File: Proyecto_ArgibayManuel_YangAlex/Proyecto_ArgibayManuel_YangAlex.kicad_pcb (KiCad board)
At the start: 2 copper layers, 60 parts, among them IC1 LM1117, J1 Conn_01x01, J2 Con_1x2, J3 Con_1x3, J4 Conn_01x03_Pin, J5 Conn_01x06, J6 Con_ICSP, J7 Conn_01x02, K1 RT314012, K2 RT314012, Q1 2N2222, Q2 2N2222, SW1 SW_Push, SW2 SW_Push, SW3 SW_Push, SW4 SW_Push, U1 PIC18F258-I_SO, U2 HDC2010YPAR, U3 LT1716IS5TRMPBF, U4 LT1716IS5TRMPBF, U5 TXS0108EPW, U6 DRV8871DDA, U7 DRV8871DDA, U8 MCP2551-I-P, X1 DB9, X2 DB9, Y1 Crystal

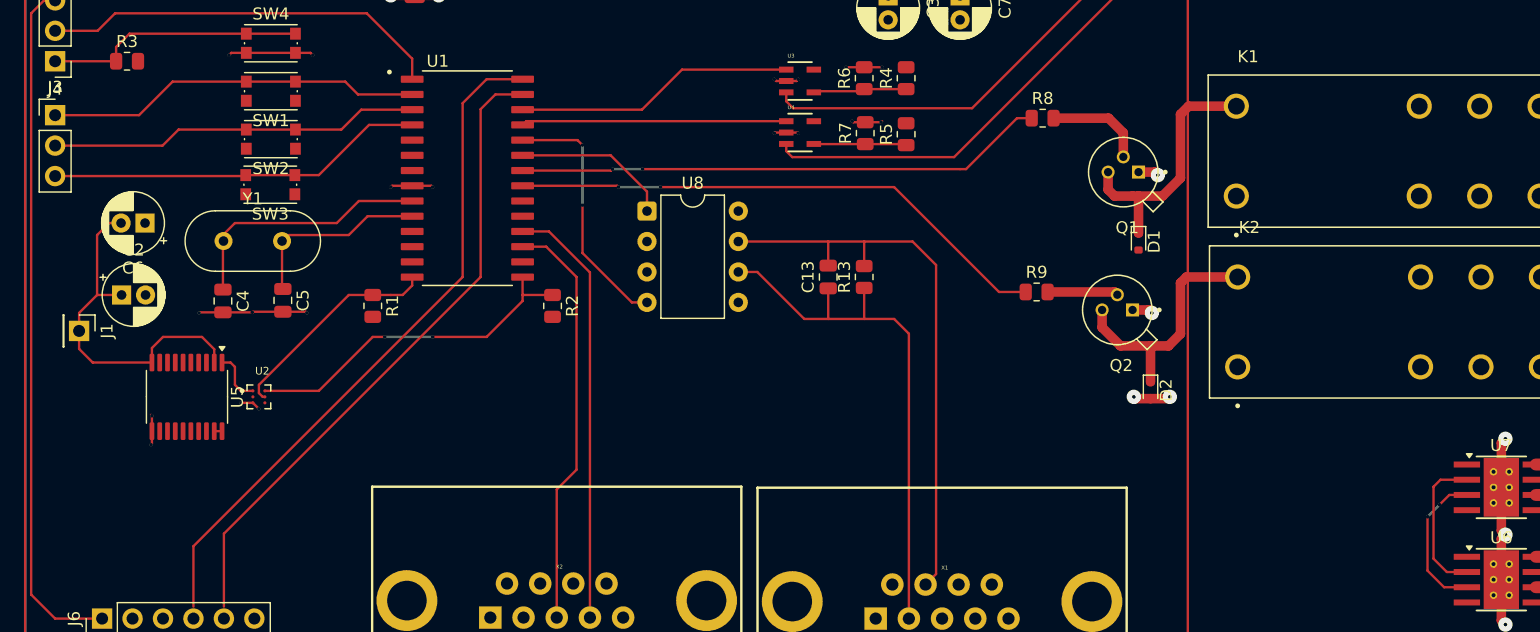
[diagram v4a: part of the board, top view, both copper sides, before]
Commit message: cambio del crystal
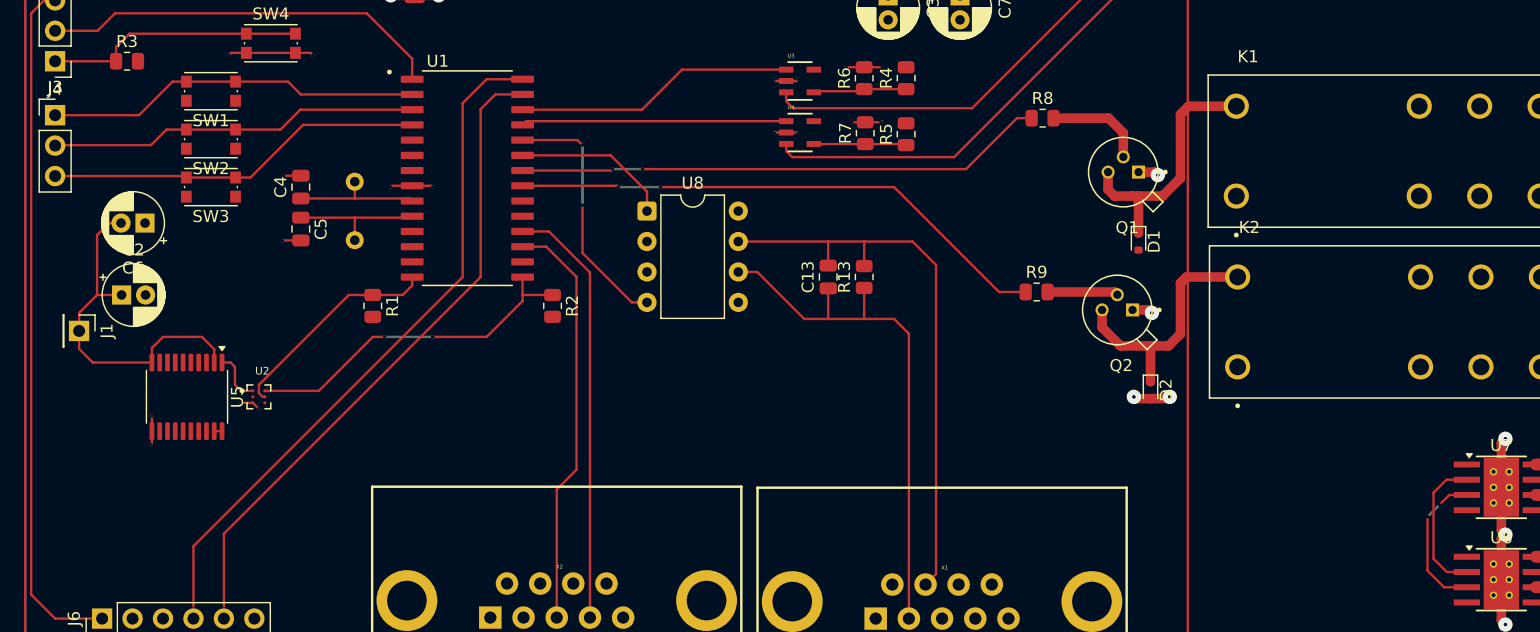
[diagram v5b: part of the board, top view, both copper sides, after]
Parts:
- Y1: moved to B.Cu
- moved Y1 12.0 mm to (125.0, 66.5), turned to -90 degrees
- moved C4 11.5 mm to (120.5, 67.0), turned to 90 degrees
- moved C5 6.14 mm to (120.5, 70.5)
- moved SW1 5.00 mm to (113.0, 59.0)
- moved SW2 5.00 mm to (113.0, 63.0)
- moved SW3 4.95 mm to (113.0, 67.0)
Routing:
- net TX1: track 21.0 -> 10.8 mm
- net GND: track 37.0 -> 30.9 mm, vias 21 -> 20
- net TX2: track 15.8 -> 11.2 mm
